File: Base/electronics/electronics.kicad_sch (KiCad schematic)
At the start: 7 parts, among them SW1 Power Switch

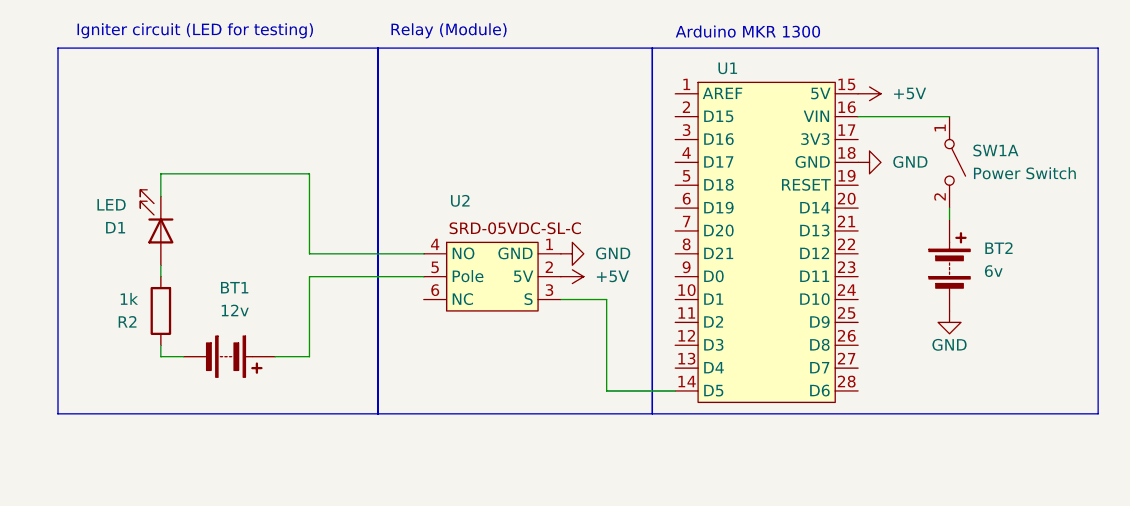
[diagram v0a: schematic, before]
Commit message: update schematic
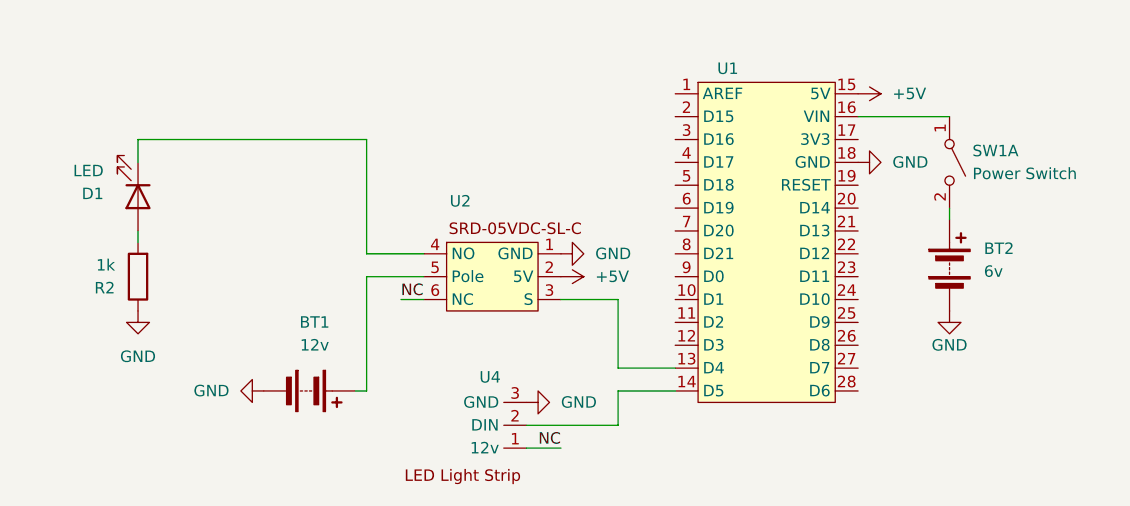
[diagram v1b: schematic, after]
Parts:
- added U4: (no value), symbol rocket:Light_strip
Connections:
- net GND: now also BT1.2 (-), R2.1, U4.3 (GND)
- net at U1.13 (D4): now also U2.3 (S)
- net at U1.14 (D5): now also U4.2 (DIN); no longer U2.3 (S)
- net NC: now reaches U2.6 (NC)
- net NC: now also U4.1 (12v)
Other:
- note removed: "Arduino MKR 1300"
- note removed: "Igniter circuit (LED for testing)"
- note removed: "Relay (Module)"
- moved on the sheet: BT1, D1, R2
